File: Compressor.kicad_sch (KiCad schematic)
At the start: 56 parts, among them J1 GND 12V, J10 AC LIVE IN, J11 Conn_01x02_Pin, J12 AC OUT 1, J15 Sensor Pins A, J16 Sensor Pins B, J2 GND(A), J3 +12V, J4 Conn_01x02_Pin, J5 Relay In Pins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

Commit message: Split up boards
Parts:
- added J13: Conn_01x06_Pin, SMD-Connectors:SMD-PinHeader_1x06_P2.54mm_Vertical, symbol Connector:Conn_01x06_Pin
- added J14: Conn_01x06_Pin, Connector_PinSocket_2.54mm:PinSocket_1x06_P2.54mm_Vertical, symbol Connector:Conn_01x06_Pin
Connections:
- net +3.3V: now also J13.5 (Pin_5), J14.5 (Pin_5)
- net +5V(A): now also J13.4 (Pin_4), J14.4 (Pin_4)
- net Current Sense: now also U6.32 (GPIO27_ADC1); no longer U6.31 (GPIO26_ADC0)
- net GND: now also J13.6 (Pin_6), J14.6 (Pin_6)
- net Pressure: now also U6.31 (GPIO26_ADC0); no longer U6.32 (GPIO27_ADC1)
- net Reset Wifi: now also J13.2 (Pin_2); no longer R11.2, SW1.2
- net Shut Down: now also J13.3 (Pin_3); no longer R17.2, SW2.2
- net Solenoid: now also U6.20 (GPIO15); no longer U6.21 (GPIO16)
- net at R21.1: now also J13.1 (Pin_1); no longer D2.4 (DIN)
- new net: D2.4 (DIN), J14.1 (Pin_1)
- new net: J14.2 (Pin_2), R11.2, SW1.2
- new net: J14.3 (Pin_3), R17.2, SW2.2
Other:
- moved on the sheet: C1, C11, C12, C13, C14, C18, C19, C2, C20, C3, C6, D1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

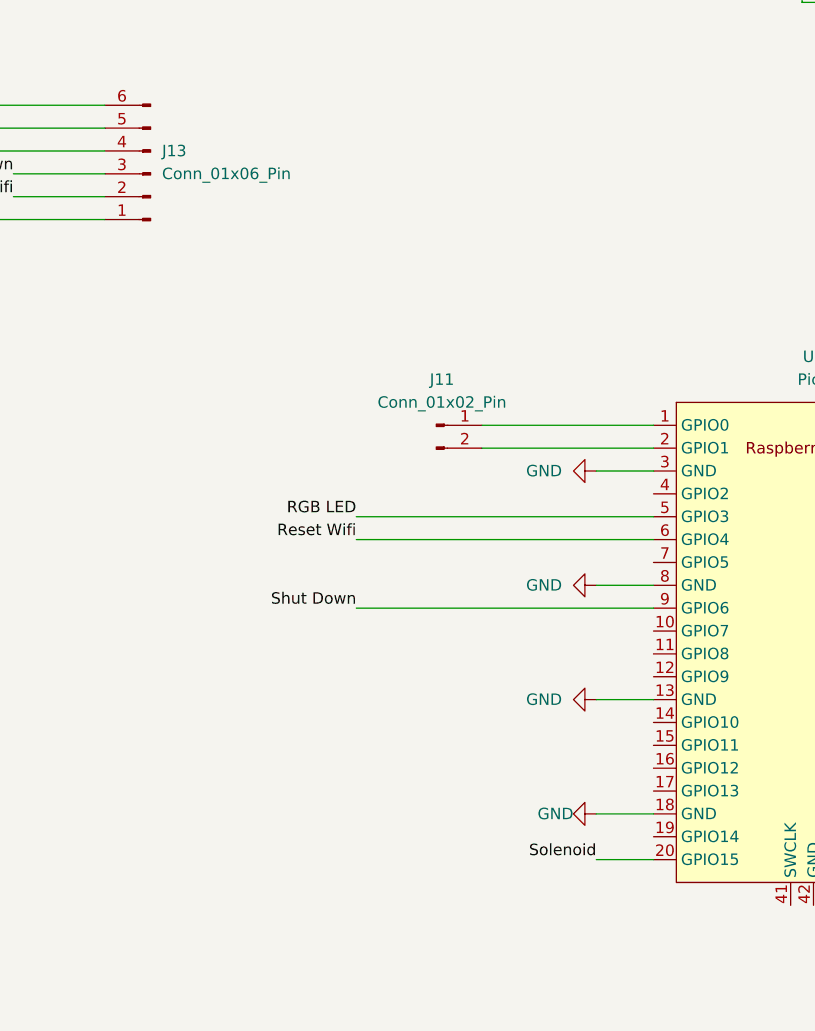
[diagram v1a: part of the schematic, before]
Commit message: Added temp sensor
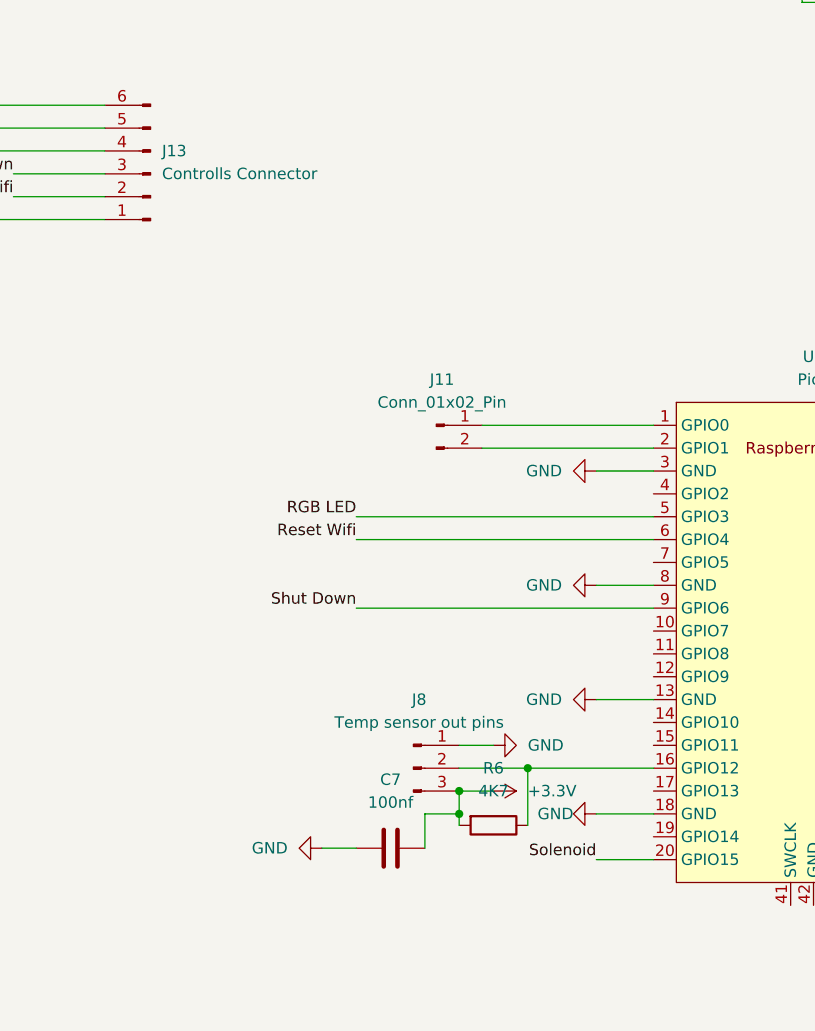
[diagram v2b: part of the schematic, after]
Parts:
- added C7: 100nf, Capacitor_SMD:C_1206_3216Metric_Pad1.33x1.80mm_HandSolder, symbol Device:C
- added J8: Temp sensor out pins, SMD-Connectors:SMD-PinHeader_1x03_P2.54mm_Vertical, symbol Connector:Conn_01x03_Pin
- added R6: 4K7, Resistor_SMD:R_1206_3216Metric_Pad1.30x1.75mm_HandSolder, symbol Device:R
- J13: value Conn_01x06_Pin -> Controlls Connector
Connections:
- net +3.3V: now also C7.2, J8.3 (Pin_3), R6.2
- net GND: now also C7.1, J8.1 (Pin_1)
- net at U6.16 (GPIO12): now also J8.2 (Pin_2), R6.1
